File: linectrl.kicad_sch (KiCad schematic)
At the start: 22 parts, among them K1 Relay_SPST-NO, K2 Relay_SPDT, Q1 PMOS, Q2 PMOS, T1 Transformer_1P_1S, U5 LM358

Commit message: finish linectrl implementation
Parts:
- added C2, C3, C4, C5, C6: 0.47u, symbol Device:C
- added D2, D4: 1N4148, Diode_THT:D_DO-35_SOD27_P7.62mm_Horizontal, symbol Diode:1N4148
- added D6, D8: D, Diode_THT:D_A-405_P12.70mm_Horizontal, symbol Device:D
- added JP2: Jumper_1-2, Jumper:SolderJumper-3_P1.3mm_Bridged2Bar12_RoundedPad1.0x1.5mm, symbol Jumper:Jumper_3_Bridged12
- added K2: Relay_SPST-NO, Relay_THT:Relay_SPST_StandexMeder_SIL_Form1A, symbol Relay:Relay_SPST-NO
- added K4: Relay_SPDT, Phones:K_AZ943-1C_AMZ, symbol Relay:Relay_SPDT
- added Q2, Q4: PMOS, Package_TO_SOT_THT:TO-92_HandSolder, symbol Simulation_SPICE:PMOS
- added R10: 19, symbol Device:R
- added R12, R16: 10k, Resistor_THT:R_Axial_DIN0207_L6.3mm_D2.5mm_P10.16mm_Horizontal, symbol Device:R
- added R14: 500, Resistor_THT:R_Axial_DIN0207_L6.3mm_D2.5mm_P10.16mm_Horizontal, symbol Device:R
- added R2, R5, R6: 10k, symbol Device:R
- added R8: 1, symbol Device:R
- added T2: Transformer_1P_1S, symbol Device:Transformer_1P_1S
- added U4, U7: (no value), symbol Phones:4C_Connector
- renumbered D3 to D1, D4 to D3, D1 to D5, D2 to D7, K2 to K3, Q2 to Q3, R4 to R1, R1 to R11, R2 to R13, R3 to R15, R5 to R3, R6 to R4, R8 to R7, R7 to R9, U4 to U6
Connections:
- net +5V: now also Q2.3 (S), Q4.3 (S), R12.1, R16.2, R5.2
- net GND: now also D1.1 (K), D3.2 (A), T1.3 (SA), C5.1, C6.1, D2.1 (K), D4.2 (A), D6.2 (A), D8.2 (A), K2.5, K4.5, R6.1, T2.3 (SA); no longer R7.1, U5.5 (+), U5.6 (-)
- net audioOut2: now reaches U5.7
- net audioOut2: now also R10.2
- net at D1.2 (A), D3.1 (K), T1.4 (SB): now also C3.1; no longer R3.1, R4.2, U5.3 (+)
- net audioOut renamed audioOut1
- net controlSW renamed controlSW1
- net hookSW renamed hookSW1
- new net: JP2.2 (C), R14.1, R2.1, U4.2
- new net: C2.1, R2.2
- new net: C4.2, R5.1, R6.2, U5.5 (+)
- new net: R10.1, R8.2, U5.6 (-)
- new net: JP2.1 (A), K4.4
- new net: JP2.3 (B), K4.3
- new net: K2.1, R14.2
- new net: D6.1 (K), K2.3, Q2.1 (D)
- new net: K2.7, T2.2 (AB), U4.3, U7.2
- new net: C2.2, T2.1 (AA)
- new net: C4.1, D2.2 (A), D4.1 (K), T2.4 (SB)
- new net: C6.2, R8.1
- new net: D8.1 (K), K4.2, Q4.1 (D)
- new net: C5.2, R7.1
- new net: C3.2, R3.1, R4.2, U5.3 (+)
- new net: U4.4, U7.1
- new net: K4.1, U7.3
- new net: U4.1, U7.4
- new net controlSW2: Q4.2 (G), R16.1
- new net hookSW2: Q2.2 (G), R12.2
- no-connect marks 1 -> 0
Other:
- note added: "Line 1 Circuitry"
- note added: "Line 2 Circuitry"
- note removed: "Line Circuitry"
- moved on the sheet: C1, D1, D3, D5, D7, JP1, K1, K3, Q1, Q3, R1, R11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

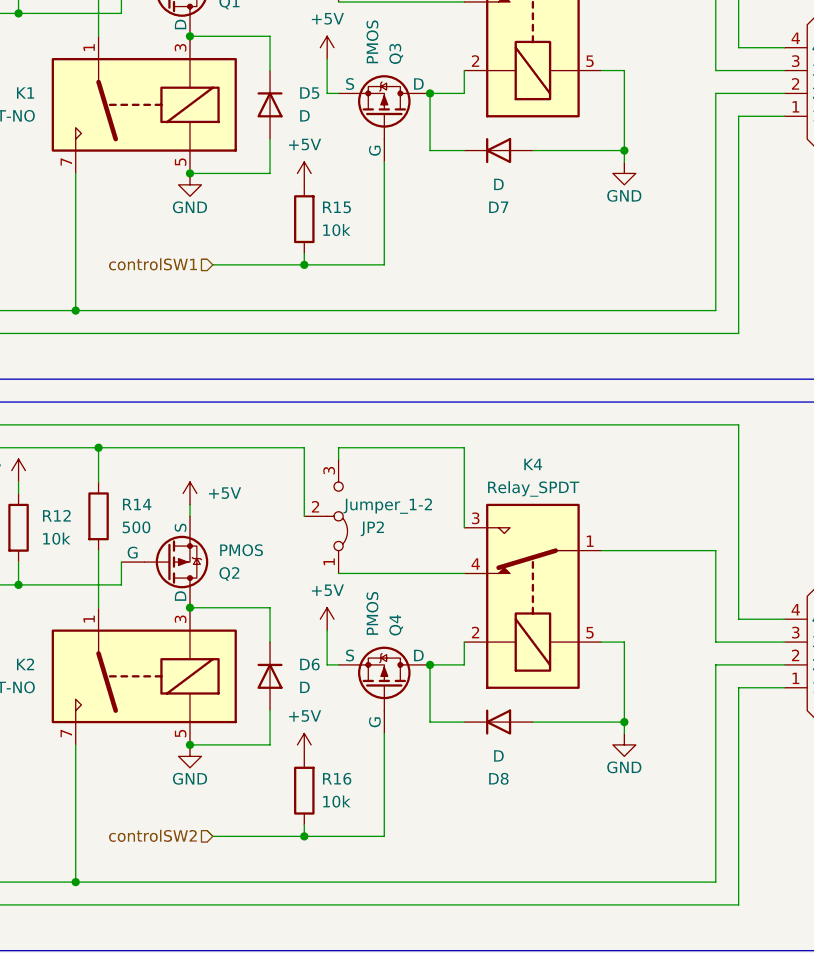
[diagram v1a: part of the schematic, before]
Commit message: add transfer buttons subsheet
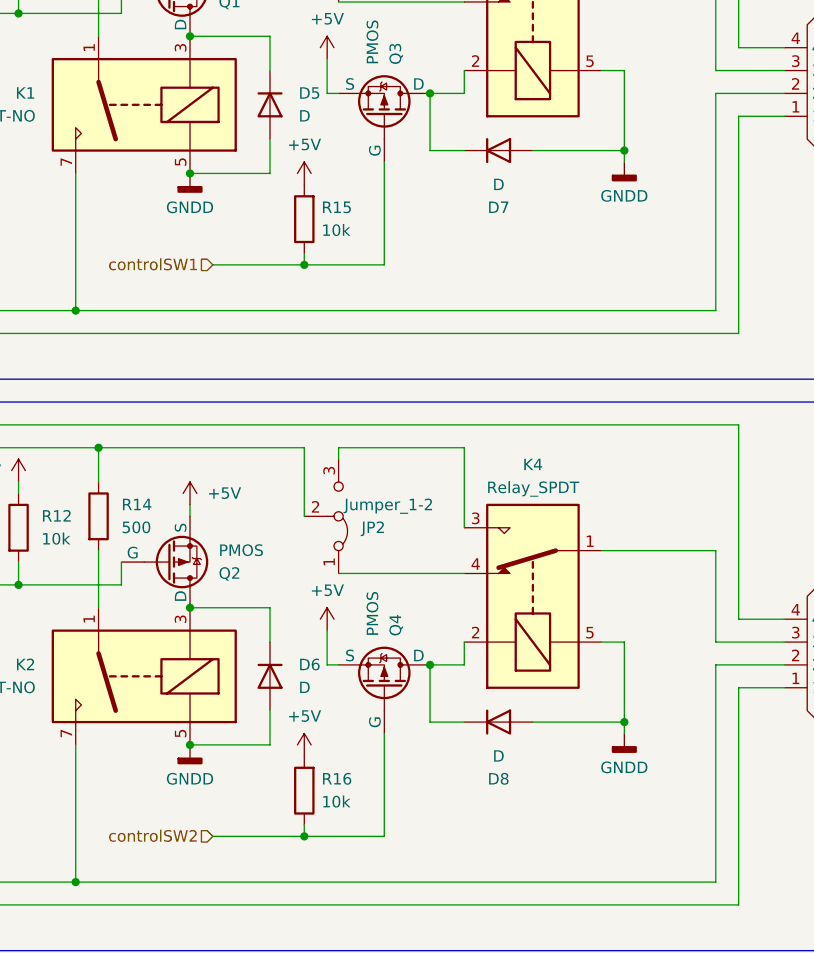
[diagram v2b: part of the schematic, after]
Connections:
- net GND: no longer D5.2 (A), D6.2 (A), D7.2 (A), D8.2 (A), K1.5, K2.5, K3.5, K4.5
- new net GNDD: D5.2 (A), D6.2 (A), D7.2 (A), D8.2 (A), K1.5, K2.5, K3.5, K4.5

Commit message: start connecting subsheets to main schematic
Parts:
- removed U3, U4, U6, U7: (no value), symbol Phones:4C_Connector
- added J1, J2, J3, J4: 6P4C, symbol Connector:6P4C
- renumbered U5 to U2
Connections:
- net GNDD: now also K1.A1, K2.A1, K3.A2, K4.A2; no longer K1.5, K2.5, K3.5, K4.5
- net at JP2.2 (C), R14.1, R2.1: now also J2.2
- net at R13.2: now also K1.13; no longer K1.1
- net at D5.1 (K), Q1.1 (D): now also K1.A2; no longer K1.3
- net at T1.2 (AB): now also K1.14, J1.3, J3.2; no longer K1.7
- net at D7.1 (K), Q3.1 (D): now also K3.A1; no longer K3.2
- net at JP1.3 (B): no longer K3.3
- net at JP1.1 (A): no longer K3.4
- net at JP2.1 (A): no longer K4.4
- net at JP2.3 (B): no longer K4.3
- net at R14.2: now also K2.13; no longer K2.1
- net at D6.1 (K), Q2.1 (D): now also K2.A2; no longer K2.3
- net at T2.2 (AB): now also K2.14, J2.3, J4.2; no longer K2.7
- net at JP1.2 (C), R1.1, R13.1: now also J1.2
- net at D8.1 (K), Q4.1 (D): now also K4.A1; no longer K4.2
- new net: J3.3, K3.11
- new net: J2.1, J4.4
- new net: J2.4, J4.1
- new net: J4.3, K4.11
- new net: J1.1, J3.4
- new net: J1.4, J3.1

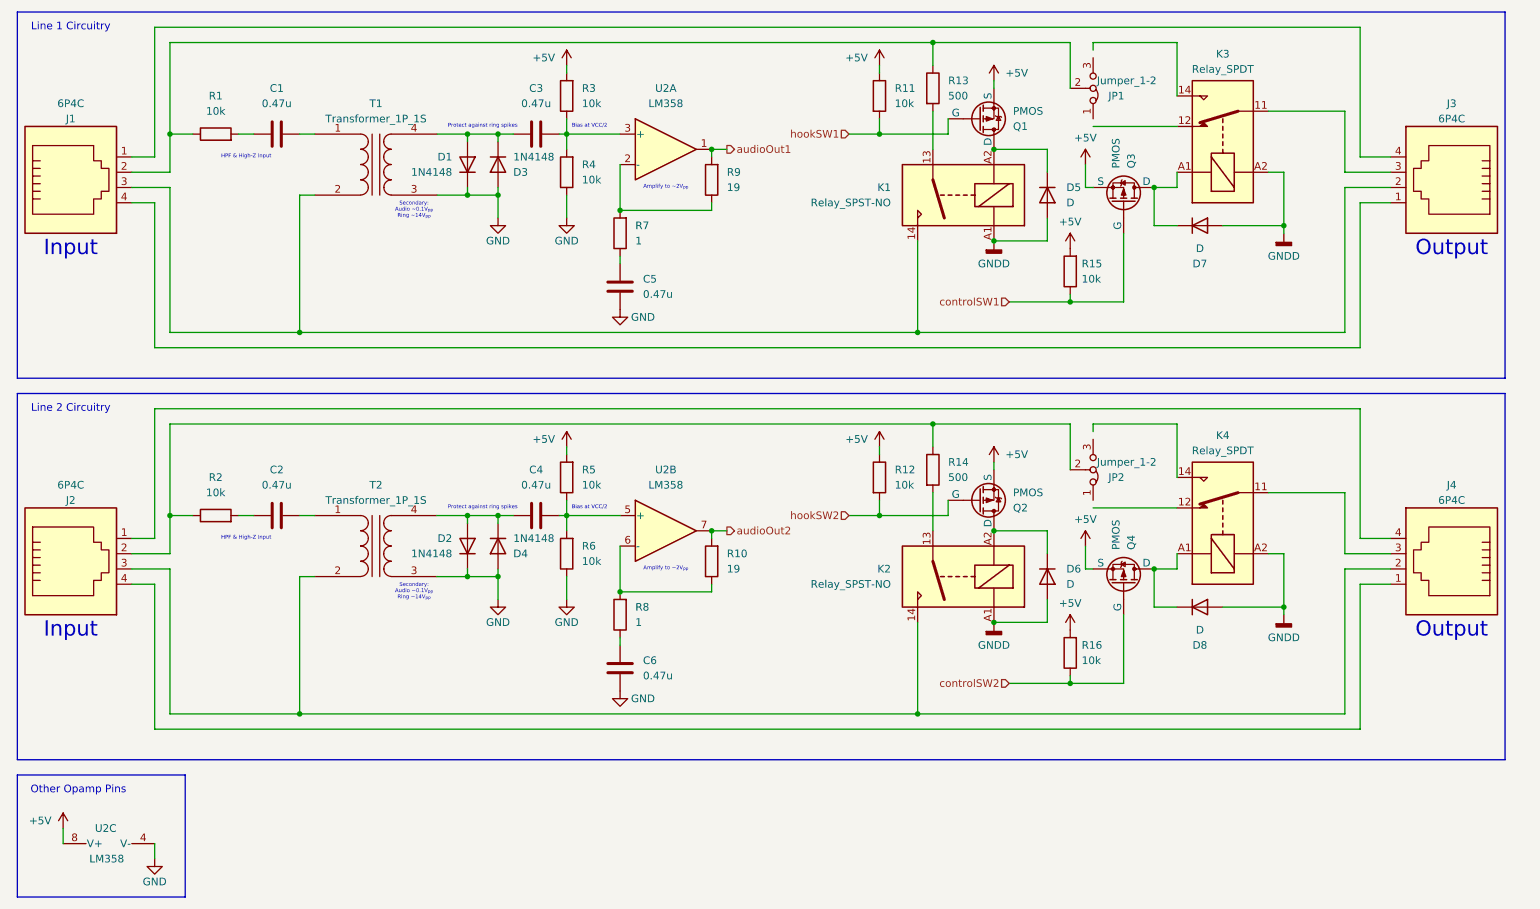
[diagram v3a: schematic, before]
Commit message: add test points throughout the schematic
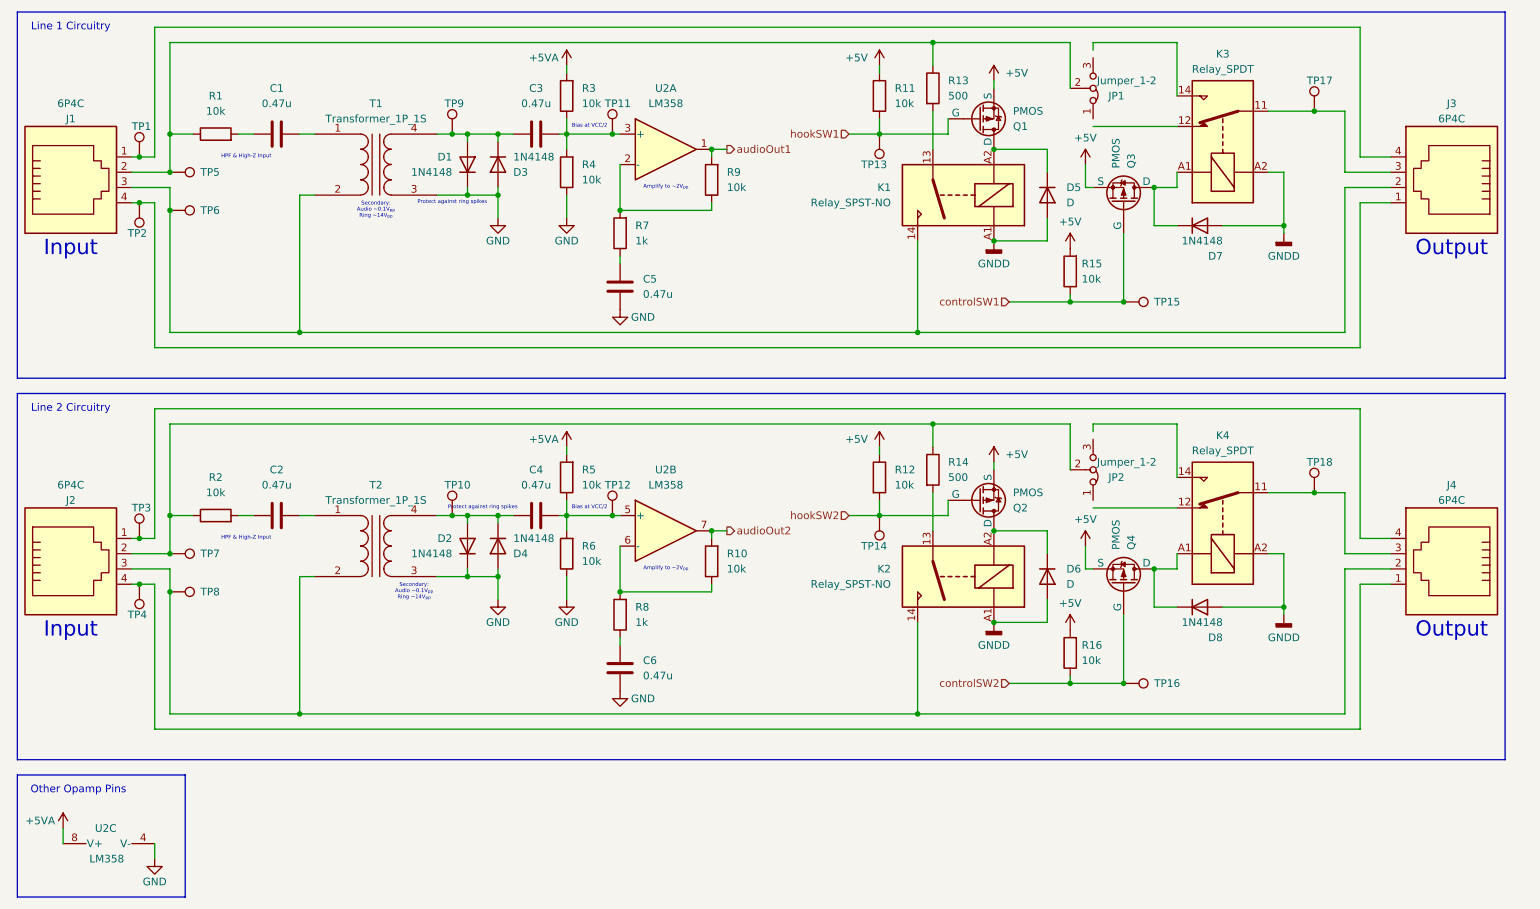
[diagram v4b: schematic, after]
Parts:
- removed D7, D8: D, Diode_THT:D_A-405_P12.70mm_Horizontal, symbol Device:D
- added D7, D8: 1N4148, Diode_THT:D_DO-35_SOD27_P7.62mm_Horizontal, symbol Diode:1N4148
- added TP1, TP10, TP11, TP12, TP13, TP14, TP15, TP16, TP17, TP18, TP2, TP3, TP4, TP5, TP6, TP7, TP8, TP9: TestPoint, Testpoints:M5_3in1_TestPoint, symbol Connector:TestPoint
- C1, C2, C3, C4, C5, C6: footprint (none) -> Capacitor_THT:C_Rect_L7.0mm_W2.0mm_P5.00mm
- R1, R2, R3, R4, R5, R6: footprint (none) -> Resistor_THT:R_Axial_DIN0207_L6.3mm_D2.5mm_P7.62mm_Horizontal
- R10, R9: value 19 -> 10k; footprint (none) -> Resistor_THT:R_Axial_DIN0207_L6.3mm_D2.5mm_P7.62mm_Horizontal
- R7, R8: value 1 -> 1k; footprint (none) -> Resistor_THT:R_Axial_DIN0207_L6.3mm_D2.5mm_P7.62mm_Horizontal
- U2: footprint (none) -> Package_DIP:DIP-8_W7.62mm
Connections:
- net +5V: no longer R3.2, R5.2, U2.8 (V+)
- net GNDD: now also D7.2 (A), D8.2 (A)
- net controlSW1: now also TP15.1
- net controlSW2: now also TP16.1
- net hookSW1: now also TP13.1
- net hookSW2: now also TP14.1
- net at J2.2, JP2.2 (C), R14.1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: now also TP7.1
- net at C4.2, R5.1, R6.2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: now also TP12.1
- net at J1.3, J3.2, K1.14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: now also TP6.1
- net at J3.3, K3.11: now also TP17.1
- net at K3.A1, Q3.1 (D): now also D7.1 (K)
- net at C3.1, D1.2 (A), D3.1 (K)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: now also TP9.1
- net at J2.3, J4.2, K2.14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: now also TP8.1
- net at C4.1, D2.2 (A), D4.1 (K)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: now also TP10.1
- net at J1.2, JP1.2 (C), R1.1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: now also TP5.1
- net at K4.A1, Q4.1 (D): now also D8.1 (K)
- net at C3.2, R3.1, R4.2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: now also TP11.1
- net at J2.1, J4.4: now also TP3.1
- net at J2.4, J4.1: now also TP4.1
- net at J4.3, K4.11: now also TP18.1
- net at J1.1, J3.4: now also TP1.1
- net at J1.4, J3.1: now also TP2.1
- new net +5VA: R3.2, R5.2, U2.8 (V+)

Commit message: finish initial schematic design, start pcb layout
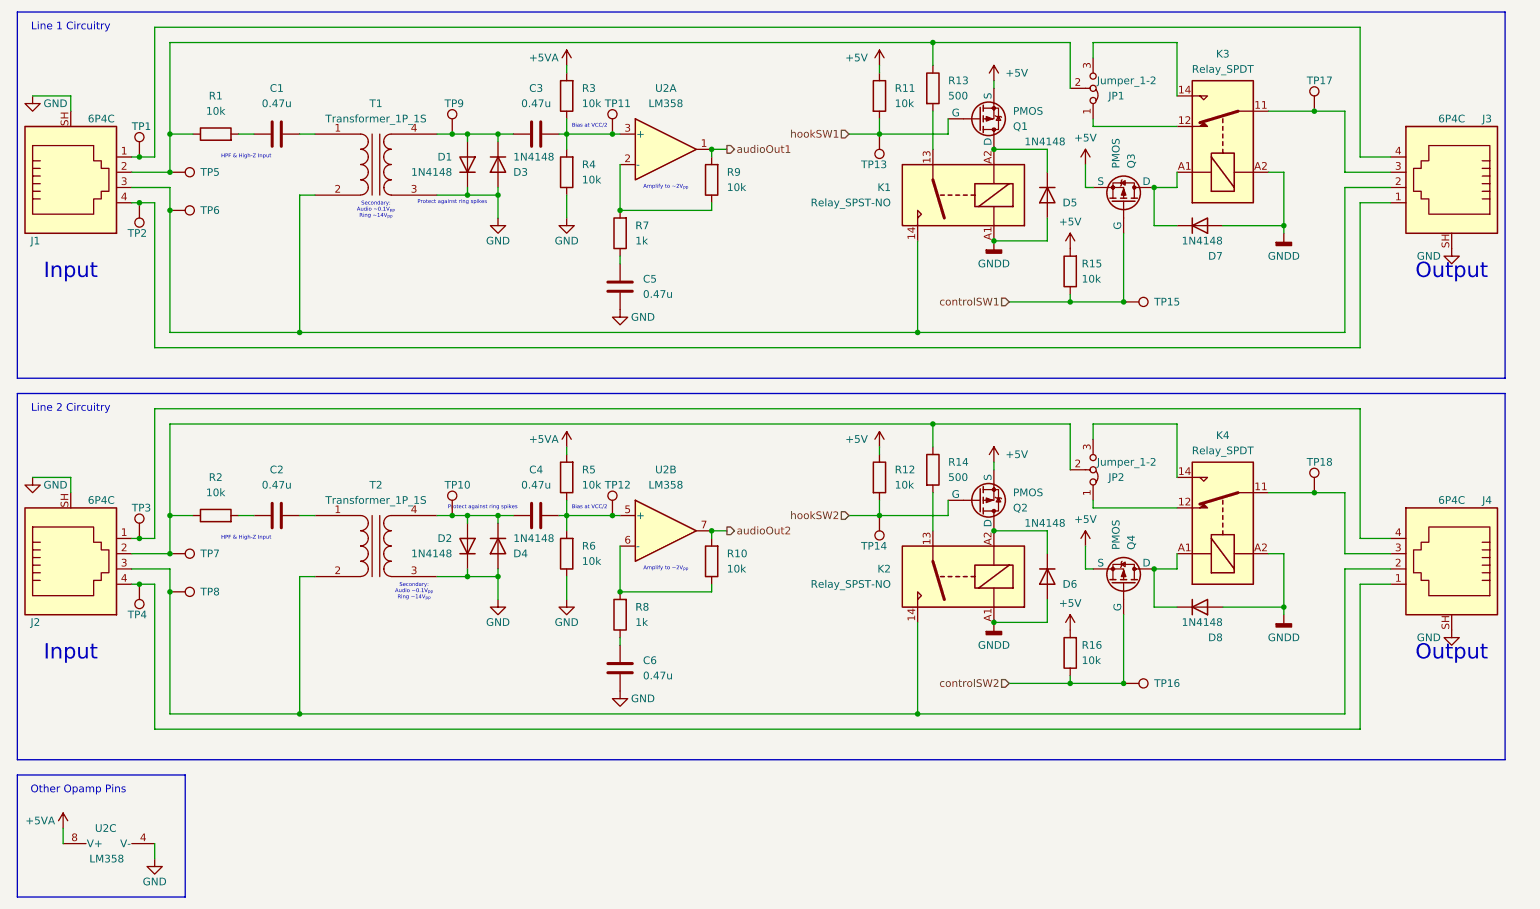
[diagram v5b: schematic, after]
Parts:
- removed D5, D6: D, Diode_THT:D_A-405_P12.70mm_Horizontal, symbol Device:D
- added D5, D6: 1N4148, Diode_THT:D_DO-35_SOD27_P7.62mm_Horizontal, symbol Diode:1N4148
- J1, J2, J3, J4: footprint (none) -> Phones:CUI_CRJ050-1-TH; symbol Connector:6P4C -> Connector:6P4C_Shielded; DKPN (none) -> 2223-CRJ050-1-TH-ND
- T1, T2: footprint (none) -> Phones:TY-145P; DKPN (none) -> 237-1121-ND
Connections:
- net GND: now also J1.SH, J2.SH, J3.SH, J4.SH
- net GNDD: now also D5.2 (A), D6.2 (A)
- net at K1.A2, Q1.1 (D): now also D5.1 (K)
- net at K3.12: now also JP1.1 (A)
- net at K3.14: now also JP1.3 (B)
- net at JP2.1 (A): now also K4.12
- net at JP2.3 (B): now also K4.14
- net at K2.A2, Q2.1 (D): now also D6.1 (K)
